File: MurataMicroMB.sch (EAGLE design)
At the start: 63 parts, among them CON1 C-2395, CON2 WM17143CT-ND, CON3 CON_MIL_10_ARM, CON4 C-2395, IC1 NC7SZ00M5XCT-ND, IC2 296-35164-1-ND, IC3 IC_LPC11U3XQFN33, IC4 AZ1117EH-3.3TRG1DICT-ND, Q1 1253-1168-1-ND, SW1 P-8073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

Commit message: update eagle version = 7.5.0; library update
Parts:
- CON1, CON4: value C-2395 -> CON_MICROSD_C2395
- CON2: device mylib:CON_USBMICROBUB -> mylib:CON_USB_UB
- IC4: value AZ1117EH-3.3TRG1DICT-ND -> LDO4_3.3_SOT223; device mylib:IC_LDO_XX1117_4 -> mylib:LDO4_3.3_SOT223
- L1: value 445-7844-1-ND -> INDUCTOR_4.7U_2016
- Q1: device mylib:CLOCK_CRYSTAL_4_3225 -> mylib:CRYSTAL4_12M_3225
- SW1, SW3: device mylib:SW_TACTSW_2PP8073 -> mylib:TACTSW2_BK_P807X
- SW2: device mylib:SW_TACTSW_2PP8073 -> mylib:TACTSW2_BL_P807X
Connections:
- net 3.3V: now also IC4.OUT/EN/NC; no longer IC4.OUT@1
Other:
- note removed: "Coilcraft PFL2010-472MEB 4.7uH/2016"
- moved on the sheet: CON2, IC4
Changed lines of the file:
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@@
 <?xml version="1.0" encoding="utf-8"?>
 <!DOCTYPE eagle SYSTEM "eagle.dtd">
-<eagle version="6.5.0">
+<eagle version="7.5.0">
 <drawing>
 <settings>
@@
 <parts>
 <part name="FRAME1" library="frames" deviceset="A4L-LOC" device=""/>
-<part name="CON1" library="mylib" deviceset="CON_MICROSD" device="_C2395" value="C-2395"/>
+<part name="CON1" library="mylib" deviceset="CON_MICROSD" device="_C2395" value="CON_MICROSD_C2395"/>
 <part name="PCB1" library="dp_pcb_local" deviceset="PCB_DP_RECTANGLE" device="-43X70" value="PCB_DP_RECTANGLE-43X70"/>
 <part name="IC1" library="74xx-little-us_local" deviceset="74*1G00" device="DBV" technology="LVC" value="NC7SZ00M5XCT-ND"/>
-<part name="CON2" library="mylib" deviceset="CON_USB" device="UB" technology="MICROB" value="WM17143CT-ND"/>
+<part name="CON2" library="mylib" deviceset="CON_USB" device="_UB" value="WM17143CT-ND"/>
 <part name="CON3" library="mylib" deviceset="CON_MIL_10" device="_ARM"/>
 <part name="SUPPLY1" library="mylib" deviceset="GND" device=""/>
@@
 <part name="SUPPLY7" library="mylib" deviceset="GND" device=""/>
 <part name="SUPPLY8" library="mylib" deviceset="GND" device=""/>
-<part name="L1" library="mylib" deviceset="INDUCTOR_" device="_2016" technology="4.7U" value="445-7844-1-ND"/>
+<part name="L1" library="mylib" deviceset="INDUCTOR_" device="_2016" technology="4.7U" value="INDUCTOR_4.7U_2016"/>
 <part name="IC2" library="mylib" deviceset="IC_DCDC_LM27313" device="" value="296-35164-1-ND"/>
 <part name="D1" library="mylib" deviceset="DIODE_SMALL" device=""/>
@@
 <part name="R8" library="mylib" deviceset="R_US_*" device="_1005" technology="10K" value="10k/1005"/>
 <part name="R9" library="mylib" deviceset="R_US_*" device="_1005" technology="10K" value="10k/1005"/>
-<part name="Q1" library="mylib" deviceset="CLOCK_CRYSTAL_4" device="_3225" value="1253-1168-1-ND"/>
+<part name="Q1" library="mylib" deviceset="CRYSTAL4_*" device="_3225" technology="12M" value="1253-1168-1-ND"/>
 <part name="C3" library="mylib" deviceset="C_SMD_*" device="_1005" technology="18P" value="18p/1005"/>
 <part name="C12" library="mylib" deviceset="C_SMD_*" device="_1005" technology="18P" value="18p/1005"/>
 <part name="SUPPLY2" library="mylib" deviceset="GND" device=""/>
-<part name="IC4" library="mylib" deviceset="IC_LDO_XX1117_4" device="" value="AZ1117EH-3.3TRG1DICT-ND"/>
+<part name="IC4" library="mylib" deviceset="LDO4_*" device="_SOT223" technology="3.3" value="LDO4_3.3_SOT223"/>
 <part name="R1" library="mylib" deviceset="R_US_*" device="_1005" technology="33R" value="33/1005"/>
 <part name="R10" library="mylib" deviceset="R_US_*" device="_1005" technology="33R" value="33/1005"/>
@@
 <part name="R12" library="mylib" deviceset="R_US_*" device="_1005" technology="10K" value="10k/1005"/>
 <part name="SUPPLY15" library="mylib" deviceset="GND" device=""/>
-<part name="SW1" library="mylib" deviceset="SW_TACTSW_2P" device="P8073" value="P-8073"/>
-<part name="SW2" library="mylib" deviceset="SW_TACTSW_2P" device="P8073" value="P-8073"/>
-<part name="SW3" library="mylib" deviceset="SW_TACTSW_2P" device="P8073" value="P-8073"/>
+<part name="SW1" library="mylib" deviceset="TACTSW2_*" device="_P807X" technology="BK" value="P-8073"/>
+<part name="SW2" library="mylib" deviceset="TACTSW2_*" device="_P807X" technology="BL" value="P-8073"/>
+<part name="SW3" library="mylib" deviceset="TACTSW2_*" device="_P807X" technology="BK" value="P-8073"/>
 <part name="SUPPLY16" library="mylib" deviceset="GND" device=""/>
 <part name="SUPPLY17" library="mylib" deviceset="GND" device=""/>
 <part name="SUPPLY18" library="mylib" deviceset="GND" device=""/>
-<part name="CON4" library="mylib" deviceset="CON_MICROSD" device="_C2395" value="C-2395"/>
+<part name="CON4" library="mylib" deviceset="CON_MICROSD" device="_C2395" value="CON_MICROSD_C2395"/>
 <part name="SUPPLY19" library="mylib" deviceset="GND" device=""/>
 <part name="C15" library="mylib" deviceset="C_SMD_*" device="_1608" technology="0.1U" value="0.1u/1608"/>
@@
 <plain>
 <text x="162.56" y="5.08" size="12.7" layer="94">r0.2</text>
-<text x="73.66" y="49.53" size="1.016" layer="94" align="center">Coilcraft
-PFL2010-472MEB
-4.7uH/2016</text>
 <text x="243.84" y="73.66" size="1.27" layer="94" rot="R90" align="center">MurataMicroSD</text>
 <text x="243.84" y="147.32" size="1.27" layer="94" rot="R90" align="center">microSD</text>
@@
 <instances>
 <instance part="FRAME1" gate="G$1" x="0" y="0"/>
-<instance part="CON1" gate="G$1" x="241.3" y="60.96"/>
+<instance part="CON1" gate="G$1" x="241.3" y="60.96">
+<attribute name="AKIZUKI" x="246.38" y="38.1" size="0.8128" layer="96" rot="R90" display="both"/>
+<attribute name="DIGIKEY" x="248.92" y="38.1" size="0.8128" layer="96" rot="R90" display="both"/>
+<attribute name="MOUSER" x="251.46" y="38.1" size="0.8128" layer="96" rot="R90" display="both"/>
+</instance>
 <instance part="PCB1" gate="G$1" x="12.7" y="10.16"/>
 <instance part="IC1" gate="A" x="193.04" y="78.74"/>
 <instance part="IC1" gate="P" x="193.04" y="78.74"/>
-<instance part="CON2" gate="G$1" x="20.32" y="134.62" rot="MR0"/>
+<instance part="CON2" gate="G$1" x="20.32" y="134.62" rot="MR0">
+<attribute name="DIGIKEY" x="20.32" y="142.24" size="0.8128" layer="96" rot="MR0" display="both"/>
+</instance>
 <instance part="CON3" gate="G$1" x="99.06" y="68.58"/>
 <instance part="SUPPLY1" gate="GND" x="33.02" y="127" rot="MR0"/>
@@
 <instance part="SUPPLY7" gate="GND" x="208.28" y="43.18"/>
 <instance part="SUPPLY8" gate="GND" x="236.22" y="27.94"/>
-<instance part="L1" gate="G$1" x="73.66" y="45.72" smashed="yes">
-<attribute name="NAME" x="71.12" y="45.466" size="1.778" layer="95" rot="R180"/>
-<attribute name="VALUE" x="71.12" y="43.688" size="1.016" layer="96"/>
+<instance part="L1" gate="G$1" x="73.66" y="45.72">
+<attribute name="DIGIKEY" x="68.58" y="48.26" size="0.8128" layer="96" display="both"/>
 </instance>
 <instance part="IC2" gate="G$1" x="73.66" y="27.94"/>
@@
 <instance part="C12" gate="G$1" x="109.22" y="93.98" rot="MR0"/>
 <instance part="SUPPLY2" gate="GND" x="109.22" y="81.28"/>
-<instance part="IC4" gate="G$1" x="160.02" y="50.8" smashed="yes">
-<attribute name="NAME" x="162.56" y="43.18" size="1.778" layer="95"/>
-<attribute name="VALUE" x="154.94" y="54.61" size="1.016" layer="96"/>
+<instance part="IC4" gate="G$1" x="160.02" y="50.8">
+<attribute name="DIGIKEY" x="147.32" y="55.88" size="0.8128" layer="96" display="both"/>
 </instance>
 <instance part="R1" gate="G$1" x="55.88" y="134.62"/>
@@
 <instance part="C14" gate="G$1" x="73.66" y="127" rot="MR0"/>
 <instance part="TR1" gate="G$1" x="48.26" y="162.56" rot="MR0"/>
-<instance part="R11" gate="G$1" x="48.26" y="149.86" rot="R270"/>
+<instance part="R11" gate="G$1" x="48.26" y="149.86" rot="R270">
+<attribute name="DIGIKEY" x="50.8" y="149.86" size="0.8128" layer="96" display="both"/>
+</instance>
 <instance part="SUPPLY9" gate="GND" x="68.58" y="114.3"/>
 <instance part="SUPPLY14" gate="GND" x="73.66" y="114.3"/>
@@
 <instance part="SUPPLY17" gate="GND" x="25.4" y="76.2"/>
 <instance part="SUPPLY18" gate="GND" x="38.1" y="76.2"/>
-<instance part="CON4" gate="G$1" x="241.3" y="132.08"/>
+<instance part="CON4" gate="G$1" x="241.3" y="132.08">
+<attribute name="AKIZUKI" x="246.38" y="109.22" size="0.8128" layer="96" rot="R90" display="both"/>
+<attribute name="DIGIKEY" x="248.92" y="109.22" size="0.8128" layer="96" rot="R90" display="both"/>
+<attribute name="MOUSER" x="251.46" y="109.22" size="0.8128" layer="96" rot="R90" display="both"/>
+</instance>
 <instance part="SUPPLY19" gate="GND" x="223.52" y="124.46" rot="R270"/>
 <instance part="C15" gate="G$1" x="213.36" y="127" rot="MR0"/>
@@
 <pinref part="IC2" gate="G$1" pin="GND"/>
 <pinref part="C4" gate="G$1" pin="2"/>
-<wire x1="60.96" y1="22.86" x2="50.8" y2="22.86" width="0.1524" layer="91"/>
+<wire x1="86.36" y1="22.86" x2="50.8" y2="22.86" width="0.1524" layer="91"/>
 <wire x1="50.8" y1="22.86" x2="45.72" y2="22.86" width="0.1524" layer="91"/>
 <wire x1="45.72" y1="22.86" x2="45.72" y2="33.02" width="0.1524" layer="91"/>
@@
 <label x="180.34" y="50.8" size="1.778" layer="95"/>
 <pinref part="IC4" gate="G$1" pin="OUT"/>
-<pinref part="IC4" gate="G$1" pin="OUT@1"/>
-<wire x1="167.64" y1="48.26" x2="170.18" y2="48.26" width="0.1524" layer="91"/>
-<wire x1="170.18" y1="48.26" x2="170.18" y2="50.8" width="0.1524" layer="91"/>
+<pinref part="IC4" gate="G$1" pin="OUT/EN/NC"/>
+<wire x1="160.02" y1="55.88" x2="170.18" y2="55.88" width="0.1524" layer="91"/>
+<wire x1="170.18" y1="55.88" x2="170.18" y2="50.8" width="0.1524" layer="91"/>
 <junction x="170.18" y="50.8"/>
 </segment>
@@
 <segment>
 <pinref part="CON2" gate="G$1" pin="SHLD"/>
-<junction x="12.7" y="129.54"/>
+<junction x="27.94" y="129.54"/>
 </segment>
 </net>
@@
 <segment>
 <pinref part="IC2" gate="G$1" pin="!SHDN!"/>
-<wire x1="60.96" y1="27.94" x2="55.88" y2="27.94" width="0.1524" layer="91"/>
+<wire x1="60.96" y1="22.86" x2="55.88" y2="27.94" width="0.1524" layer="91"/>
 <pinref part="R2" gate="G$1" pin="1"/>
 <wire x1="55.88" y1="27.94" x2="55.88" y2="33.02" width="0.1524" layer="91"/>
@@
 <pinref part="IC2" gate="G$1" pin="FB"/>
 <pinref part="R3" gate="G$1" pin="1"/>
-<wire x1="86.36" y1="22.86" x2="101.6" y2="22.86" width="0.1524" layer="91"/>
+<wire x1="86.36" y1="27.94" x2="101.6" y2="22.86" width="0.1524" layer="91"/>
 <wire x1="101.6" y1="22.86" x2="101.6" y2="25.4" width="0.1524" layer="91"/>
 <pinref part="R4" gate="G$1" pin="2"/>

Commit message: library update
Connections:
- net !CS!: no longer R5.2
- net SCK: now also R5.2
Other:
- moved on the sheet: IC2
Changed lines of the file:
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@@
 <part name="TP8" library="testpad_local" deviceset="TP" device="PAD1-13"/>
 <part name="TP9" library="testpad_local" deviceset="TP" device="PAD1-13"/>
+<part name="SUPPLY25" library="mylib" deviceset="GND" device=""/>
 </parts>
 <sheets>
@@
 <attribute name="DIGIKEY" x="68.58" y="48.26" size="0.8128" layer="96" display="both"/>
 </instance>
-<instance part="IC2" gate="G$1" x="73.66" y="27.94"/>
+<instance part="IC2" gate="G$1" x="73.66" y="22.86"/>
 <instance part="D1" gate="G$1" x="91.44" y="45.72"/>
 <instance part="R2" gate="G$1" x="55.88" y="35.56" rot="R90"/>
@@
 <instance part="TP8" gate="G$1" x="124.46" y="45.72" rot="R270"/>
 <instance part="TP9" gate="G$1" x="124.46" y="12.7" rot="R270"/>
+<instance part="SUPPLY25" gate="GND" x="86.36" y="12.7"/>
 </instances>
 <busses>
@@
 </segment>
 <segment>
+<pinref part="SUPPLY25" gate="GND" pin="GND"/>
 <pinref part="IC2" gate="G$1" pin="GND"/>
+<wire x1="86.36" y1="15.24" x2="86.36" y2="17.78" width="0.1524" layer="91"/>
+</segment>
+<segment>
 <pinref part="C4" gate="G$1" pin="2"/>
-<wire x1="86.36" y1="22.86" x2="50.8" y2="22.86" width="0.1524" layer="91"/>
 <wire x1="50.8" y1="22.86" x2="45.72" y2="22.86" width="0.1524" layer="91"/>
 <wire x1="45.72" y1="22.86" x2="45.72" y2="33.02" width="0.1524" layer="91"/>
@@
 <pinref part="C7" gate="G$1" pin="2"/>
 <wire x1="50.8" y1="33.02" x2="50.8" y2="22.86" width="0.1524" layer="91"/>
-<junction x="50.8" y="22.86"/>
 </segment>
 <segment>
@@
 <label x="170.18" y="114.3" size="1.778" layer="95"/>
 </segment>
+<segment>
+<wire x1="182.88" y1="93.98" x2="175.26" y2="93.98" width="0.1524" layer="91"/>
+<pinref part="R5" gate="G$1" pin="2"/>
+<label x="182.88" y="93.98" size="1.778" layer="95"/>
+</segment>
 </net>
 <net name="MISO" class="0">
@@
 <wire x1="228.6" y1="73.66" x2="215.9" y2="73.66" width="0.1524" layer="91"/>
 <label x="215.9" y="73.66" size="1.778" layer="95"/>
-</segment>
-<segment>
-<wire x1="182.88" y1="93.98" x2="175.26" y2="93.98" width="0.1524" layer="91"/>
-<pinref part="R5" gate="G$1" pin="2"/>
-<label x="182.88" y="93.98" size="1.778" layer="95"/>
 </segment>
 <segment>
@@
 <wire x1="71.12" y1="45.72" x2="60.96" y2="45.72" width="0.1524" layer="91"/>
 <pinref part="IC2" gate="G$1" pin="VIN"/>
-<wire x1="60.96" y1="45.72" x2="60.96" y2="33.02" width="0.1524" layer="91"/>
+<wire x1="60.96" y1="45.72" x2="60.96" y2="27.94" width="0.1524" layer="91"/>
 <wire x1="60.96" y1="45.72" x2="55.88" y2="45.72" width="0.1524" layer="91"/>
 <junction x="60.96" y="45.72"/>
@@
 <pinref part="IC2" gate="G$1" pin="LX"/>
 <wire x1="76.2" y1="45.72" x2="86.36" y2="45.72" width="0.1524" layer="91"/>
-<wire x1="86.36" y1="45.72" x2="86.36" y2="33.02" width="0.1524" layer="91"/>
+<wire x1="86.36" y1="45.72" x2="86.36" y2="27.94" width="0.1524" layer="91"/>
 <pinref part="D1" gate="G$1" pin="A"/>
 <wire x1="86.36" y1="45.72" x2="88.9" y2="45.72" width="0.1524" layer="91"/>
@@
 <segment>
 <pinref part="IC2" gate="G$1" pin="!SHDN!"/>
-<wire x1="60.96" y1="22.86" x2="55.88" y2="27.94" width="0.1524" layer="91"/>
+<wire x1="60.96" y1="17.78" x2="55.88" y2="17.78" width="0.1524" layer="91"/>
 <pinref part="R2" gate="G$1" pin="1"/>
-<wire x1="55.88" y1="27.94" x2="55.88" y2="33.02" width="0.1524" layer="91"/>
+<wire x1="55.88" y1="17.78" x2="55.88" y2="33.02" width="0.1524" layer="91"/>
 </segment>
 </net>
@@
 <pinref part="IC2" gate="G$1" pin="FB"/>
 <pinref part="R3" gate="G$1" pin="1"/>
-<wire x1="86.36" y1="27.94" x2="101.6" y2="22.86" width="0.1524" layer="91"/>
+<wire x1="86.36" y1="22.86" x2="101.6" y2="22.86" width="0.1524" layer="91"/>
 <wire x1="101.6" y1="22.86" x2="101.6" y2="25.4" width="0.1524" layer="91"/>
 <pinref part="R4" gate="G$1" pin="2"/>

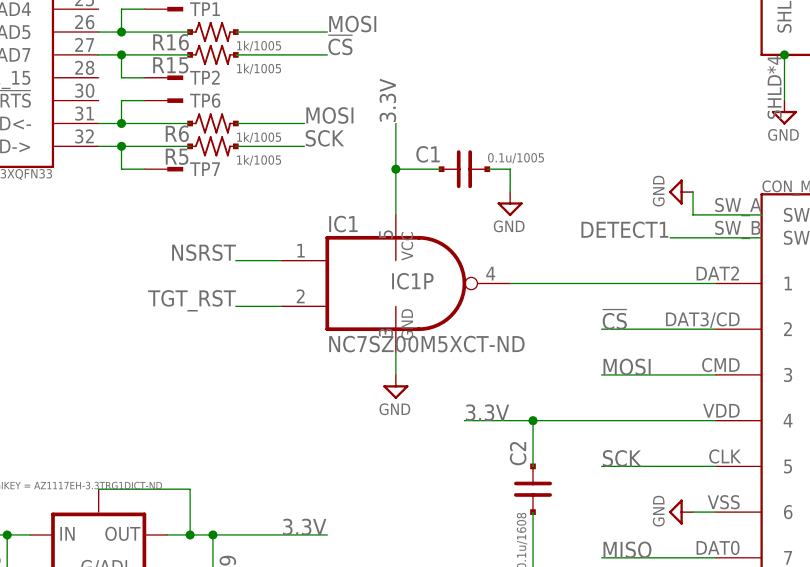
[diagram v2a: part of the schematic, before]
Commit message: [ MB ] TP1,2,6,7 changed to use test pin; related Rs movee
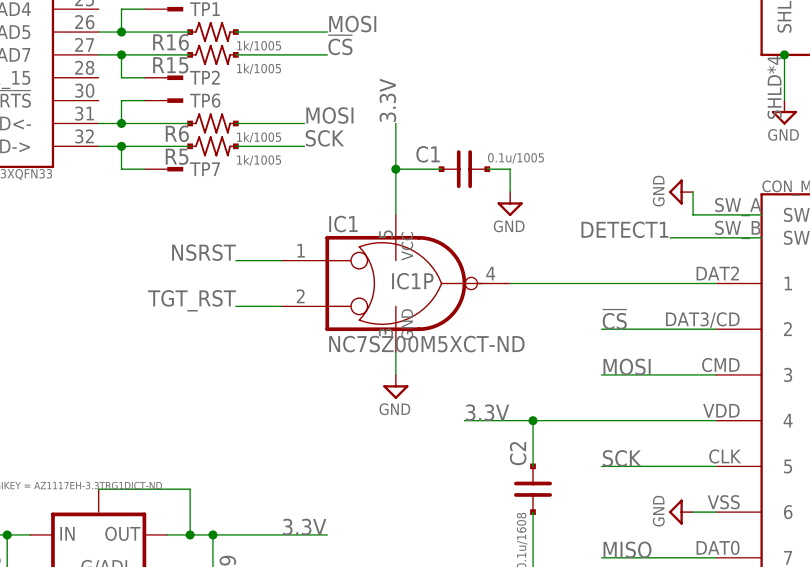
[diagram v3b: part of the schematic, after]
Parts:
- TP1, TP2, TP6, TP7: value TESTPAD -> TESTPAD_1608; device mylib:TESTPAD -> mylib:TESTPAD_1608
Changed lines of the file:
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@@
 <part name="R19" library="mylib" deviceset="R_US_*" device="_1005" technology="10K" value="10k/1005"/>
 <part name="R20" library="mylib" deviceset="R_US_*" device="_1005" technology="10K" value="10k/1005"/>
-<part name="TP1" library="mylib" deviceset="TESTPAD" device=""/>
-<part name="TP2" library="mylib" deviceset="TESTPAD" device=""/>
-<part name="TP6" library="mylib" deviceset="TESTPAD" device=""/>
-<part name="TP7" library="mylib" deviceset="TESTPAD" device=""/>
+<part name="TP1" library="mylib" deviceset="TESTPAD" device="_1608" value="TESTPAD_1608"/>
+<part name="TP2" library="mylib" deviceset="TESTPAD" device="_1608" value="TESTPAD_1608"/>
+<part name="TP6" library="mylib" deviceset="TESTPAD" device="_1608" value="TESTPAD_1608"/>
+<part name="TP7" library="mylib" deviceset="TESTPAD" device="_1608" value="TESTPAD_1608"/>
 <part name="TP8" library="testpad_local" deviceset="TP" device="PAD1-13"/>
 <part name="TP9" library="testpad_local" deviceset="TP" device="PAD1-13"/>
@@
 P0_2
 *BL = P0_14*</text>
+<circle x="188.976" y="81.28" radius="0.915809375" width="0.1524" layer="94"/>
+<circle x="188.976" y="76.2" radius="0.915809375" width="0.1524" layer="94"/>
+<wire x1="188.976" y1="82.804" x2="188.976" y2="74.676" width="0.1524" layer="94" curve="-90"/>
+<wire x1="188.976" y1="82.804" x2="198.12" y2="78.74" width="0.1524" layer="94" curve="-90"/>
+<wire x1="198.12" y1="78.74" x2="188.976" y2="74.676" width="0.1524" layer="94" curve="-90"/>
+<wire x1="198.12" y1="78.74" x2="202.692" y2="78.74" width="0.1524" layer="94"/>
+<wire x1="185.42" y1="81.28" x2="187.96" y2="81.28" width="0.1524" layer="94"/>
+<wire x1="185.42" y1="76.2" x2="187.96" y2="76.2" width="0.1524" layer="94"/>
 </plain>
 <instances>

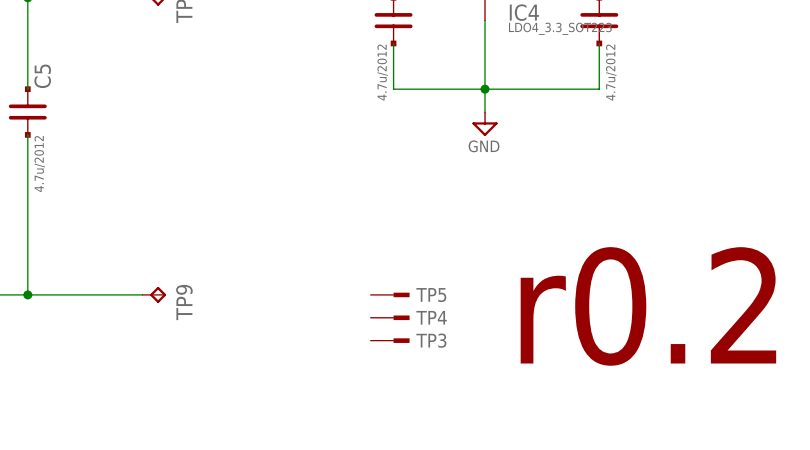
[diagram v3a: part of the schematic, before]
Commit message: [ MB ] Fiducials renamed; moved TPs
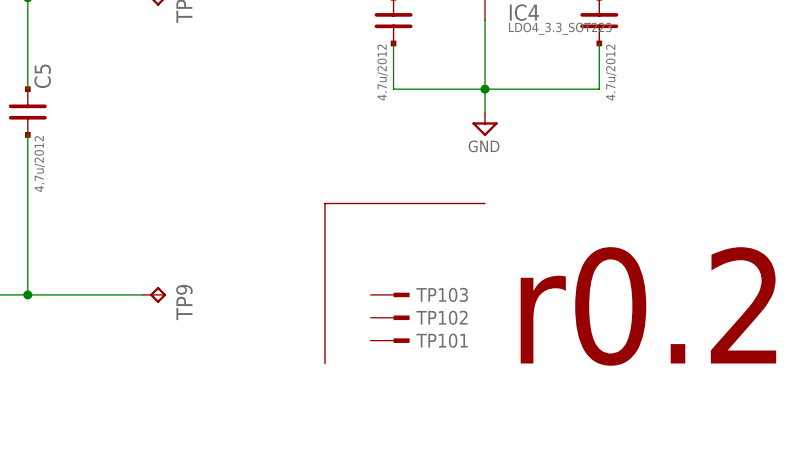
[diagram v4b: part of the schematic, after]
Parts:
- renumbered TP3 to TP101, TP4 to TP102, TP5 to TP103
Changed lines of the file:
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@@
 <part name="R15" library="mylib" deviceset="R_US_*" device="_1005" technology="1.0K" value="1k/1005"/>
 <part name="R16" library="mylib" deviceset="R_US_*" device="_1005" technology="1.0K" value="1k/1005"/>
-<part name="TP3" library="mylib" deviceset="TESTPAD" device="_F"/>
-<part name="TP4" library="mylib" deviceset="TESTPAD" device="_F"/>
-<part name="TP5" library="mylib" deviceset="TESTPAD" device="_F"/>
+<part name="TP101" library="mylib" deviceset="TESTPAD" device="_F"/>
+<part name="TP102" library="mylib" deviceset="TESTPAD" device="_F"/>
+<part name="TP103" library="mylib" deviceset="TESTPAD" device="_F"/>
 <part name="R17" library="mylib" deviceset="R_US_*" device="_1005" technology="10K" value="10k/1005"/>
 <part name="R18" library="mylib" deviceset="R_US_*" device="_1005" technology="10K" value="10k/1005"/>
@@
 <wire x1="185.42" y1="81.28" x2="187.96" y2="81.28" width="0.1524" layer="94"/>
 <wire x1="185.42" y1="76.2" x2="187.96" y2="76.2" width="0.1524" layer="94"/>
+<wire x1="160.02" y1="22.86" x2="142.24" y2="22.86" width="0.1524" layer="94"/>
+<wire x1="142.24" y1="22.86" x2="142.24" y2="5.08" width="0.1524" layer="94"/>
 </plain>
 <instances>
@@
 <instance part="R15" gate="G$1" x="172.72" y="104.14"/>
 <instance part="R16" gate="G$1" x="172.72" y="106.68"/>
-<instance part="TP3" gate="1" x="149.86" y="7.62"/>
-<instance part="TP4" gate="1" x="149.86" y="10.16"/>
-<instance part="TP5" gate="1" x="149.86" y="12.7"/>
+<instance part="TP101" gate="1" x="149.86" y="7.62"/>
+<instance part="TP102" gate="1" x="149.86" y="10.16"/>
+<instance part="TP103" gate="1" x="149.86" y="12.7"/>
 <instance part="R17" gate="G$1" x="114.3" y="76.2"/>
 <instance part="R18" gate="G$1" x="114.3" y="68.58"/>
